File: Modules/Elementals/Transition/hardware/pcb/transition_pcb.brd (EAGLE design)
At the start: 17.8 x 105.1 mm, 10 parts, among them J1 WQP-PJ398SM6, J2 WQP-PJ398SM6, J3 WQP-PJ398SM6, J4 WQP-PJ398SM6, J5 WQP-PJ398SM6, J6 WQP-PJ398SM6

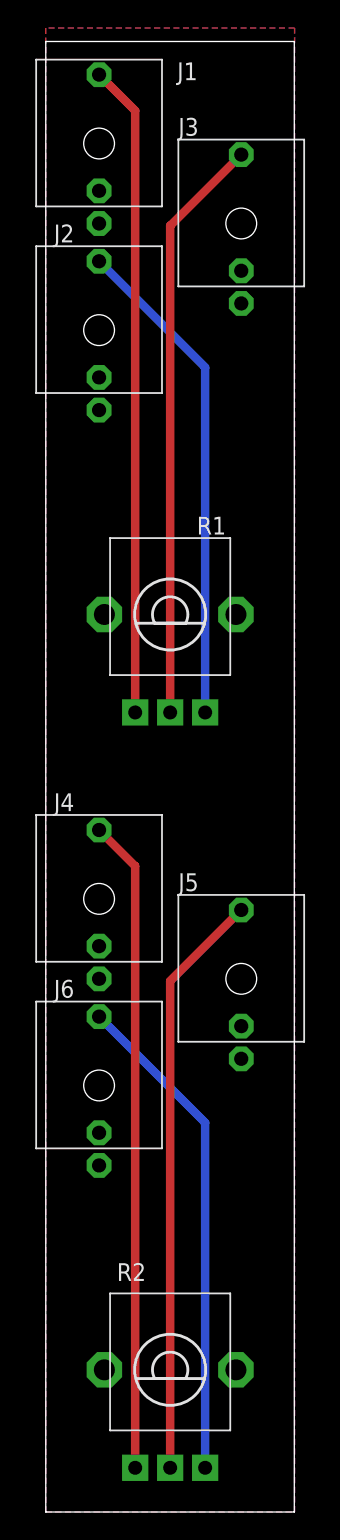
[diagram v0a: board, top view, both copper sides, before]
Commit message: Finished Transition p2
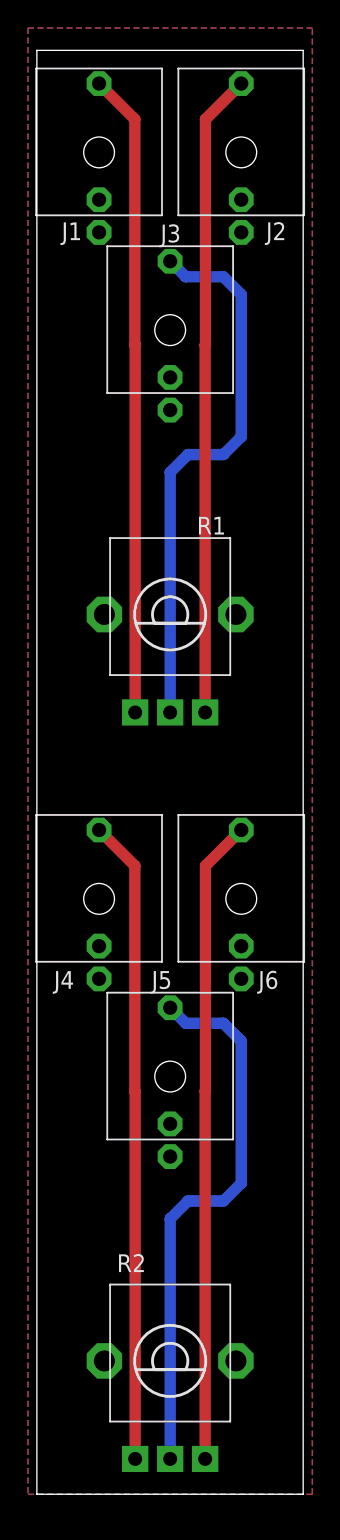
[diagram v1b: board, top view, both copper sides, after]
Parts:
- moved J6 16.8 mm to (15.2, 54.6)
- moved J2 16.3 mm to (15.2, 108.0)
- moved J3 9.16 mm to (10.2, 95.2)
- moved J5 8.64 mm to (10.2, 41.9)
- moved R2 0.64 mm to (10.2, 21.6)
- moved J1 0.63 mm to (5.08, 108.0)
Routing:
- net N$1: track 35.4 -> 46.0 mm
- net N$7: track 35.4 -> 46.0 mm
- net N$2: track 42.0 -> 39.5 mm
- net N$8: track 42.0 -> 39.5 mm
- net N$6: track 46.6 -> 46.0 mm
- net N$4: track 46.6 -> 46.0 mm
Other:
- board size 17.8 x 105.1 mm -> 19 x 103.2 mm
- board text added: "Sonic Athame is fully open-hardware and open-software! Find schematics, code, PCBs, and build instructions at sonic-athame.com"
- board text removed: "Sonic Athame is fully open-hardware and open-software! Find schematics and code on the official GitHub: github.com/nimaid/Sonic-Athame-eurorack"
